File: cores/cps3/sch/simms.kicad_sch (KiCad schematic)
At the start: 12 parts

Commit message: main_obj
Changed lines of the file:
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@@
     (effects (font (size 1.27 1.27)) (justify left))
   )
-  (hierarchical_label "R_MAINB[20..0]" (shape output) (at 335.28 135.89 0)
+  (hierarchical_label "OAM_A[20..0]" (shape output) (at 335.28 135.89 0)
     (effects (font (size 1.27 1.27)) (justify left))
   )
@@
     (effects (font (size 1.27 1.27)) (justify right))
   )
-  (hierarchical_label "R_MAINA[20..0]" (shape output) (at 381 142.24 0)
+  (hierarchical_label "OAMB_A[20..0]" (shape output) (at 381 142.24 0)
     (effects (font (size 1.27 1.27)) (justify left))
   )

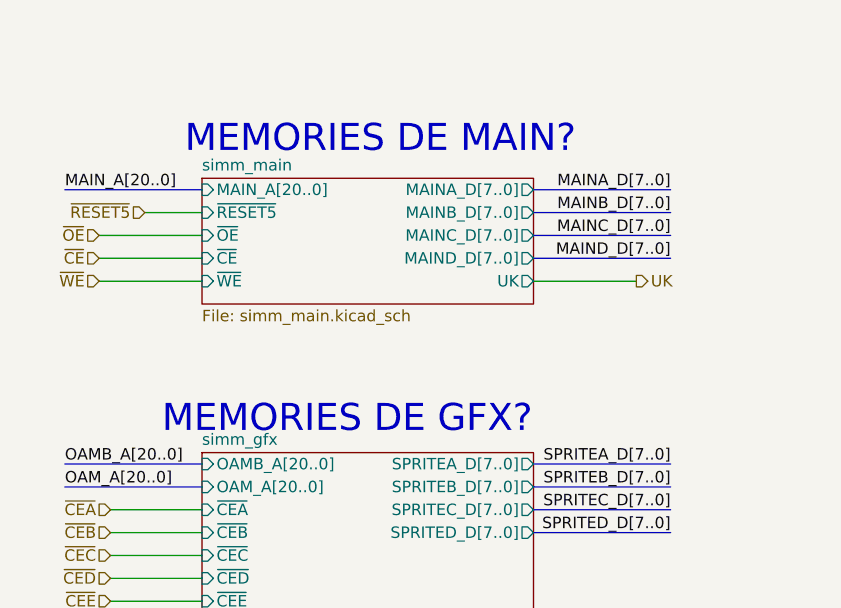
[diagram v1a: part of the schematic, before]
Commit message: new_symbols
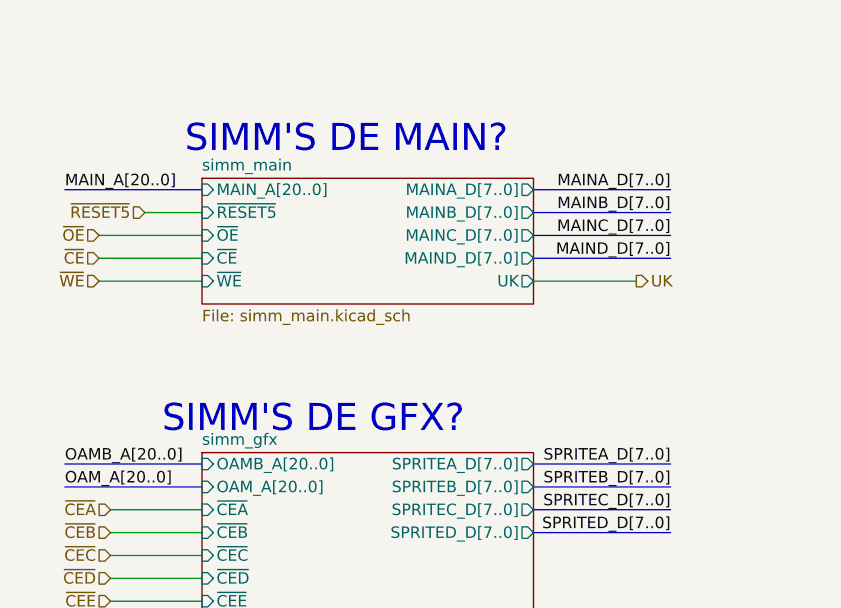
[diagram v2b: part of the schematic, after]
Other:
- note added: "SIMM'S DE GFX?"
- note added: "SIMM'S DE MAIN?"
- note removed: "MEMORIES DE GFX?"
- note removed: "MEMORIES DE MAIN?"
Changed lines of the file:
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@@
     (effects (font (size 1.27 1.27)) (justify right bottom))
   )
-  (text "MEMORIES DE MAIN?" (at 61.595 38.1 0)
+  (text "SIMM'S DE MAIN?" (at 61.595 38.1 0)
     (effects (font (size 3 3)) (justify left bottom))
   )
@@
     (effects (font (size 1.27 1.27)) (justify left bottom))
   )
-  (text "MEMORIES DE GFX?" (at 59.055 69.215 0)
+  (text "SIMM'S DE GFX?" (at 59.055 69.215 0)
     (effects (font (size 3 3)) (justify left bottom))
   )

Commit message: update6_cps
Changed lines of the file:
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@@
     (comment 1 "E.Triana")
   )
+  (junction (at 149.86 40.64) (diameter 0) (color 0 0 0 0)
+  )
   (junction (at 295.91 232.41) (diameter 0) (color 0 0 0 0)
   )
@@
     (stroke (width 0) (type default) (color 0 0 0 0))
   )
+  (wire (pts (xy 374.65 205.74) (xy 374.65 233.68))
+    (stroke (width 0) (type default) (color 0 0 0 0))
+  )
   (wire (pts (xy 53.34 80.01) (xy 63.5 80.01))
     (stroke (width 0) (type default) (color 0 0 0 0))
@@
     (stroke (width 0) (type default) (color 0 0 0 0))
   )
-  (wire (pts (xy 359.41 205.74) (xy 369.57 205.74))
+  (wire (pts (xy 359.41 205.74) (xy 374.65 205.74))
     (stroke (width 0) (type default) (color 0 0 0 0))
   )
@@
     (stroke (width 0) (type default) (color 0 0 0 0))
   )
+  (wire (pts (xy 149.86 31.75) (xy 149.86 40.64))
+    (stroke (width 0) (type default) (color 0 0 0 0))
+  )
   (wire (pts (xy 293.37 168.91) (xy 283.21 168.91))
     (stroke (width 0) (type default) (color 0 0 0 0))
@@
     (pin "9")
   )
+  (symbol (lib_id "power:VSS") (at 374.65 233.68 180) (unit 1)
+    (in_bom yes) (on_board yes)
+    (property "Reference" "#PWR?" (id 0) (at 374.65 229.87 0)
+      (effects (font (size 1.27 1.27)) hide)
+    )
+    (property "Value" "VSS" (id 1) (at 374.65 237.49 0))
+    (property "Footprint" "" (id 2) (at 374.65 233.68 0)
+      (effects (font (size 1.27 1.27)) hide)
+    )
+    (property "Datasheet" "" (id 3) (at 374.65 233.68 0)
+      (effects (font (size 1.27 1.27)) hide)
+    )
+    (pin "1")
+  )
   (symbol (lib_id "Connector:Conn_01x36_Male") (at 207.01 83.82 0) (mirror y) (unit 1)
     (in_bom yes) (on_board yes)
@@
     (pin "9")
   )
+  (symbol (lib_id "power:VCC") (at 149.86 31.75 0) (unit 1)
+    (in_bom yes) (on_board yes)
+    (property "Reference" "#PWR?" (id 0) (at 149.86 35.56 0)
+      (effects (font (size 1.27 1.27)) hide)
+    )
+    (property "Value" "VCC" (id 1) (at 149.86 27.94 0))
+    (property "Footprint" "" (id 2) (at 149.86 31.75 0)
+      (effects (font (size 1.27 1.27)) hide)
+    )
+    (property "Datasheet" "" (id 3) (at 149.86 31.75 0)
+      (effects (font (size 1.27 1.27)) hide)
+    )
+    (pin "1")
+  )
   (symbol (lib_id "Connector:Conn_01x36_Male") (at 144.78 83.82 0) (unit 1)

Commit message: clear_sch_hk_cr
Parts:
- removed SIMM1E (x2), SIMM2D (x2): Conn_01x36_Male, symbol Connector:Conn_01x36_Male
- added SIMM1E (x2), SIMM2D (x2): Conn_01x36_Male, symbol Connector:Conn_01x36_Male
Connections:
- net OAM_A19: now also SIMM4DD.3 (Pin_3); no longer SIMM4DD.4 (Pin_4)
- net OAM_A20: now also SIMM4DD.4 (Pin_4); no longer SIMM4DD.3 (Pin_3)
- net UK: now also SIMM1E.33 (Pin_33), SIMM2D.33 (Pin_33)
- net VCC: now also SIMM1E.1 (Pin_1), SIMM1E.2 (Pin_2), SIMM2D.1 (Pin_1), SIMM2D.2 (Pin_2)
- net VSS: now also SIMM1E.11 (Pin_11), SIMM1E.13 (Pin_13), SIMM1E.20 (Pin_20), SIMM1E.25 (Pin_25), SIMM1E.27 (Pin_27), SIMM1E.29 (Pin_29), SIMM1E.32 (Pin_32), SIMM2D.11 (Pin_11), SIMM2D.13 (Pin_13), SIMM2D.20 (Pin_20), SIMM2D.25 (Pin_25), SIMM2D.27 (Pin_27), SIMM2D.29 (Pin_29), SIMM2D.32 (Pin_32)
- net ~{CE}: now also SIMM1E.31 (Pin_31), SIMM2D.31 (Pin_31)
- net ~{OE}: now also SIMM1E.35 (Pin_35), SIMM2D.35 (Pin_35)
- net ~{RESET5}: now also SIMM1E.26 (Pin_26), SIMM2D.26 (Pin_26)
- net ~{WE}: now also SIMM1E.34 (Pin_34), SIMM2D.34 (Pin_34)
- new net GFXA_D0: SIMM1E.10 (Pin_10), SIMM2D.10 (Pin_10)
- new net GFXA_D1: SIMM1E.9 (Pin_9), SIMM2D.9 (Pin_9)
- new net GFXA_D2: SIMM1E.8 (Pin_8), SIMM2D.8 (Pin_8)
- new net GFXA_D3: SIMM1E.7 (Pin_7), SIMM2D.7 (Pin_7)
- new net GFXA_D4: SIMM1E.6 (Pin_6), SIMM2D.6 (Pin_6)
- new net GFXA_D5: SIMM1E.5 (Pin_5), SIMM2D.5 (Pin_5)
- new net GFXA_D6: SIMM1E.4 (Pin_4), SIMM2D.4 (Pin_4)
- new net GFXA_D7: SIMM1E.3 (Pin_3), SIMM2D.3 (Pin_3)
- new net GFXB_D0: SIMM1E.19 (Pin_19), SIMM2D.19 (Pin_19)
- new net GFXB_D1: SIMM1E.18 (Pin_18), SIMM2D.18 (Pin_18)
- new net GFXB_D2: SIMM1E.17 (Pin_17), SIMM2D.17 (Pin_17)
- new net GFXB_D3: SIMM1E.16 (Pin_16), SIMM2D.16 (Pin_16)
- new net GFXB_D4: SIMM1E.15 (Pin_15), SIMM2D.15 (Pin_15)
- new net GFXB_D5: SIMM1E.14 (Pin_14), SIMM2D.14 (Pin_14)
- new net GFXB_D6: SIMM1E.13 (Pin_13), SIMM2D.13 (Pin_13)
- new net GFXB_D7: SIMM1E.12 (Pin_12), SIMM2D.12 (Pin_12)
- new net GFXC_D0: SIMM1E.28 (Pin_28), SIMM2D.28 (Pin_28)
- new net GFXC_D1: SIMM1E.27 (Pin_27), SIMM2D.27 (Pin_27)
- new net GFXC_D2: SIMM1E.26 (Pin_26), SIMM2D.26 (Pin_26)
- new net GFXC_D3: SIMM1E.25 (Pin_25), SIMM2D.25 (Pin_25)
- new net GFXC_D4: SIMM1E.24 (Pin_24), SIMM2D.24 (Pin_24)
- new net GFXC_D5: SIMM1E.23 (Pin_23), SIMM2D.23 (Pin_23)
- new net GFXC_D6: SIMM1E.22 (Pin_22), SIMM2D.22 (Pin_22)
- new net GFXC_D7: SIMM1E.21 (Pin_21), SIMM2D.21 (Pin_21)
- new net GFXD_D0: SIMM1E.1 (Pin_1), SIMM2D.1 (Pin_1)
- new net GFXD_D1: SIMM1E.36 (Pin_36), SIMM2D.36 (Pin_36)
- new net GFXD_D2: SIMM1E.35 (Pin_35), SIMM2D.35 (Pin_35)
- new net GFXD_D3: SIMM1E.34 (Pin_34), SIMM2D.34 (Pin_34)
- new net GFXD_D4: SIMM1E.33 (Pin_33), SIMM2D.33 (Pin_33)
- new net GFXD_D5: SIMM1E.32 (Pin_32), SIMM2D.32 (Pin_32)
- new net GFXD_D6: SIMM1E.31 (Pin_31), SIMM2D.31 (Pin_31)
- new net GFXD_D7: SIMM1E.30 (Pin_30), SIMM2D.30 (Pin_30)
- new net GFX_A0: SIMM1E.24 (Pin_24), SIMM2D.24 (Pin_24)
- new net GFX_A1: SIMM1E.23 (Pin_23), SIMM2D.23 (Pin_23)
- new net GFX_A10: SIMM1E.14 (Pin_14), SIMM2D.14 (Pin_14)
- new net GFX_A11: SIMM1E.12 (Pin_12), SIMM2D.12 (Pin_12)
- new net GFX_A12: SIMM1E.11 (Pin_11), SIMM2D.11 (Pin_11)
- new net GFX_A13: SIMM1E.10 (Pin_10), SIMM2D.10 (Pin_10)
- new net GFX_A14: SIMM1E.9 (Pin_9), SIMM2D.9 (Pin_9)
- new net GFX_A15: SIMM1E.8 (Pin_8), SIMM2D.8 (Pin_8)
- new net GFX_A16: SIMM1E.7 (Pin_7), SIMM2D.7 (Pin_7)
- new net GFX_A17: SIMM1E.6 (Pin_6), SIMM2D.6 (Pin_6)
- new net GFX_A18: SIMM1E.5 (Pin_5), SIMM2D.5 (Pin_5)
- new net GFX_A19: SIMM1E.4 (Pin_4), SIMM2D.4 (Pin_4)
- new net GFX_A2: SIMM1E.22 (Pin_22), SIMM2D.22 (Pin_22)
- new net GFX_A20: SIMM1E.3 (Pin_3), SIMM2D.3 (Pin_3)
- new net GFX_A3: SIMM1E.21 (Pin_21), SIMM2D.21 (Pin_21)
- new net GFX_A4: SIMM1E.20 (Pin_20), SIMM2D.20 (Pin_20)
- new net GFX_A5: SIMM1E.19 (Pin_19), SIMM2D.19 (Pin_19)
- new net GFX_A6: SIMM1E.18 (Pin_18), SIMM2D.18 (Pin_18)
- new net GFX_A7: SIMM1E.17 (Pin_17), SIMM2D.17 (Pin_17)
- new net GFX_A8: SIMM1E.16 (Pin_16), SIMM2D.16 (Pin_16)
- new net GFX_A9: SIMM1E.15 (Pin_15), SIMM2D.15 (Pin_15)
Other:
- sheet simm_gfx renamed simms_6~3
- sheet simm_main renamed simms_2~1
- sheet simms_2~1: file simm_main.kicad_sch -> simms_2~1.kicad_sch
- sheet simms_2~1 ports: added GFXA_D[7..0], GFXB_D[7..0], GFXC_D[7..0], GFXD_D[7..0], GFX_A[20..0]; removed MAINA_D[7..0], MAINB_D[7..0], MAINC_D[7..0], MAIND_D[7..0], MAIN_A[20..0]
- sheet simms_6~3: file simm_gfx.kicad_sch -> simms_6~3.kicad_sch
- note added: "Slot 1"
- note added: "Slot 2"
- note added: "Slot 3"
- note added: "Slot 4"
- note added: "Slot 5"
- note added: "Slot 6"
- note added: "Slot Male"
- note removed: "REVISAR POSIBLE CORTO ENTRE VCC Y VSS"
- note removed: "SIMM'S DE GFX?"
- note removed: "SIMM'S DE MAIN?"

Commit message: wip_ccu
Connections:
- net Slot _M_P72: now reaches SIMM5CC.36 (Pin_36)
- net Slot _M_P72: now also SIMM1E.36 (Pin_36), SIMM2D.36 (Pin_36), SIMM3EE.36 (Pin_36), SIMM4DD.36 (Pin_36), SIMM6BB.36 (Pin_36)
- no-connect marks 81 -> 79
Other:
- moved on the sheet: SIMM6BB

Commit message: wip_ccu_gll2_cassette
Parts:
- removed SIMM1E (x2), SIMM2D (x2), SIMM3E, SIMM3EE, SIMM4D, SIMM4DD, SIMM5C, SIMM5CC, SIMM6B, SIMM6BB: Conn_01x36_Male, symbol Connector:Conn_01x36_Male
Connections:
- no-connect marks 79 -> 0
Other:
- added sheet slot_male (slot_male.kicad_sch)
- added sheet slots_female (slots_females.kicad_sch)
- note removed: "37"
- note removed: "38"
- note removed: "39 40"
- note removed: "41 42"
- note removed: "43 44"
- note removed: "45 46"
- note removed: "47 48"
- note removed: "49 50"
- note removed: "51 52"
- note removed: "53 54"
- note removed: "55 56"
- note removed: "57 58"
- note removed: "59 60"
- note removed: "61 62"
- note removed: "63 64"
- note removed: "65 66"
- note removed: "67 68"
- note removed: "69 70"
- note removed: "71 72"
- note removed: "Slot 1"
- note removed: "Slot 2"
- note removed: "Slot 3"
- note removed: "Slot 4"
- note removed: "Slot 5"
- note removed: "Slot 6"
- note removed: "Slot Male"
- note removed: "[37..72]"

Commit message: wip_ccu_cassette
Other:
- sheet slot_male ports: added UK, ~{CEA}, ~{CEB}, ~{CEC}, ~{CED}, ~{CEE}, ~{CEF}, ~{CEG}, ~{CEH}, ~{CEI}, ~{CEJ}, ~{CEK}, ~{CEL}, ~{CEM}, ~{CEN}, ~{CEO}, ~{CEP}, ~{CE}, ~{OEB}, ~{OEC}, ~{OED}, ~{OEE}, ~{OE}, ~{RESET1}, ~{RESET2}, ~{RESET3}, ~{RESET4}, ~{RESET5}, ~{WEB}, ~{WEC}, ~{WED}, ~{WEE}, ~{WE}; removed none

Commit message: wip_cassette
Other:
- sheet slot_male renamed simm_connector
- sheet simm_connector: file slot_male.kicad_sch -> simm_connector.kicad_sch
- sheet simm_connector ports: added GFX_A21, UK_CCU, ~{CE_}S1, ~{CE}_S2, ~{OE}_CCU, ~{WE}_CCU; removed UK, ~{OE}, ~{WE}
- sheet simms_2~1 ports: added UK_CCU, ~{CE_}S1, ~{CE_}S2, ~{OE}_CCU, ~{WE}_CCU; removed UK, ~{CE}, ~{OE}, ~{WE}
- sheet slots_female ports: added GFX_A21, UK_CCU, ~{CE_}S1, ~{CE}_S2, ~{OE}_CCU, ~{WE}_CCU; removed UK, ~{OE}, ~{WE}
